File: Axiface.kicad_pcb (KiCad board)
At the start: 2 copper layers, 55.4 x 36.3 mm, 30 parts, among them J1 Conn_01x02, J10 Conn_01x03, J11 Conn_01x04, J2 Conn_01x03, J3 Conn_01x03, J4 Conn_01x03, J5 Conn_01x03, J6 Conn_01x03, J7 Conn_01x03, J8 Conn_01x03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

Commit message: Mise à jour du schéma et pcb
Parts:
- added H1: MountingHole_Pad, MountingHole:MountingHole_2.7mm_M2.5_Pad, F.Cu at (91.7, 132.3)
- added H2: MountingHole_Pad, MountingHole:MountingHole_2.7mm_M2.5_Pad, F.Cu at (91.7, 100.8)
- added H3: MountingHole_Pad, MountingHole:MountingHole_2.7mm_M2.5_Pad, F.Cu at (146.1, 100.8)
- added H4: MountingHole_Pad, MountingHole:MountingHole_2.7mm_M2.5_Pad, F.Cu at (146.1, 132.3)
- C1, C4, C5, C6, C7: moved to F.Cu
- U3, U4, U5: footprint Converter_DCDC:Converter_DCDC_TRACO_TSR-1_THT -> Convert_DCDC:Converter_DCDC_TRACO_TSR-2_THT
- moved C4 20.6 mm to (113.2, 123.2)
- moved C5 15.8 mm to (145.0, 107.7), turned to 270 degrees
- moved C7 15.3 mm to (144.8, 126.5)
- moved C6 15.3 mm to (144.8, 115.4)
- moved C1 3.98 mm to (110.0, 111.0), turned to 0 degrees
- moved J8 1.65 mm to (126.1, 106.9)
- moved J5 1.57 mm to (140.3, 106.9)
- moved J2 1.53 mm to (133.2, 106.9)
- moved D1 1.27 mm to (98.4, 103.4)
- moved J3 1.09 mm to (126.1, 119.3)
- moved R2 1.02 mm to (104.3, 103.4)
- moved R3 1.02 mm to (104.3, 116.1)
- moved R4 1.02 mm to (104.3, 128.8)
- moved J9 0.97 mm to (140.3, 119.3)
- moved J6 0.90 mm to (133.2, 119.3)
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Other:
- board size 55.4 x 36.3 mm -> 60.8 x 37.8 mm

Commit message: Mise à jour avant routage
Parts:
- R2, R3, R4: value R -> 1.8k
- moved D3 2.03 mm to (98.9, 130.9)
- moved R4 2.03 mm to (104.3, 130.8)
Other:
- board text added: "-"
- board text added: "Direction"
- board text added: "RX_CPU"
- board text added: "TX_CPU"
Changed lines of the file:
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@@
   (general
     (thickness 1.6)
-    (drawings 13)
+    (drawings 17)
     (tracks 0)
     (zones 0)
@@
     (35 F.Paste user)
     (36 B.SilkS user)
-    (37 F.SilkS user)
+    (37 F.SilkS user hide)
     (38 B.Mask user)
     (39 F.Mask user)
@@
     (tags capacitor)
     (attr smd)
-    (fp_text reference C2 (at -3.432 0) (layer B.SilkS)
+    (fp_text reference C2 (at -0.13 -2.032) (layer B.SilkS)
       (effects (font (size 1 1) (thickness 0.15)) (justify mirror))
     )
@@
     (tags capacitor)
     (attr smd)
-    (fp_text reference C3 (at 3.302 0) (layer B.SilkS)
+    (fp_text reference C3 (at 3.556 0) (layer B.SilkS)
       (effects (font (size 1 1) (thickness 0.15)) (justify mirror))
     )
@@
   )
   (module LED_SMD:LED_1206_3216Metric (layer F.Cu)
-    (at 98.936 128.828)
+    (at 98.936 130.86)
     (descr "LED SMD 1206 (3216 Metric), square (rectangular) end terminal, IPC_7351 nominal, (Body size source: http://www.tortai-tech.com/upload/download/2011102023233369053.pdf), generated with kicad-footprint-generator")
     (tags diode)
     (attr smd)
-    (fp_text reference D3 (at 0 -1.82) (layer F.SilkS)
+    (fp_text reference D3 (at -0.13 1.982) (layer F.SilkS)
       (effects (font (size 1 1) (thickness 0.15)))
     )
@@
       (effects (font (size 1 1) (thickness 0.15)))
     )
-    (fp_text user - (at -4 0 90) (layer F.SilkS)
+    (fp_text user - (at 0 3.81 90) (layer F.SilkS)
       (effects (font (size 1.5 1.5) (thickness 0.15)))
     )
-    (fp_text user + (at 9 0 90) (layer F.SilkS)
+    (fp_text user + (at 5.08 3.81 90) (layer F.SilkS)
       (effects (font (size 1.5 1.5) (thickness 0.15)))
     )
@@
     (tags resistor)
     (attr smd)
-    (fp_text reference R1 (at -3.172 0) (layer B.SilkS)
+    (fp_text reference R1 (at 3.686 0) (layer B.SilkS)
       (effects (font (size 1 1) (thickness 0.15)) (justify mirror))
     )
@@
       (effects (font (size 1 1) (thickness 0.15)))
     )
-    (fp_text value R (at 0 1.82) (layer F.Fab)
+    (fp_text value 1.8k (at 0 1.82) (layer F.Fab)
       (effects (font (size 1 1) (thickness 0.15)))
     )
@@
       (effects (font (size 1 1) (thickness 0.15)))
     )
-    (fp_text value R (at 0 1.82) (layer F.Fab)
+    (fp_text value 1.8k (at 0 1.82) (layer F.Fab)
       (effects (font (size 1 1) (thickness 0.15)))
     )
@@
   )
   (module Resistor_SMD:R_1206_3216Metric (layer F.Cu)
-    (at 104.27 128.778)
+    (at 104.27 130.81)
     (descr "Resistor SMD 1206 (3216 Metric), square (rectangular) end terminal, IPC_7351 nominal, (Body size source: http://www.tortai-tech.com/upload/download/2011102023233369053.pdf), generated with kicad-footprint-generator")
     (tags resistor)
     (attr smd)
-    (fp_text reference R4 (at 0 -1.82) (layer F.SilkS)
-      (effects (font (size 1 1) (thickness 0.15)))
-    )
-    (fp_text value R (at 0 1.82) (layer F.Fab)
+    (fp_text reference R4 (at 0 2.032) (layer F.SilkS)
+      (effects (font (size 1 1) (thickness 0.15)))
+    )
+    (fp_text value 1.8k (at 0 1.82) (layer F.Fab)
       (effects (font (size 1 1) (thickness 0.15)))
     )
@@
     (tags "CMS SOT")
     (attr smd)
-    (fp_text reference U1 (at 3.404 4.166) (layer B.SilkS)
+    (fp_text reference U1 (at 3.404 4.674) (layer B.SilkS)
       (effects (font (size 1 1) (thickness 0.15)) (justify mirror))
     )
@@
       (effects (font (size 1 1) (thickness 0.15)) (justify mirror))
     )
-    (fp_text user %R (at 0 0 270) (layer B.Fab)
+    (fp_text user %R (at 0 0) (layer B.Fab)
       (effects (font (size 0.8 0.8) (thickness 0.12)) (justify mirror))
     )
@@
       (net 2 GND))
   )
+  (gr_text RX_CPU (at 99.568 127.254) (layer F.SilkS)
+    (effects (font (size 1 1) (thickness 0.1)))
+  )
+  (gr_text TX_CPU (at 99.568 124.714) (layer F.SilkS)
+    (effects (font (size 1 1) (thickness 0.1)))
+  )
+  (gr_text Direction (at 99.822 121.92) (layer F.SilkS)
+    (effects (font (size 1 1) (thickness 0.1)))
+  )
+  (gr_text - (at 97.79 119.634 180) (layer F.SilkS)
+    (effects (font (size 1.5 1.5) (thickness 0.3)))
+  )
   (dimension 31.4579 (width 0.15) (layer Dwgs.User)

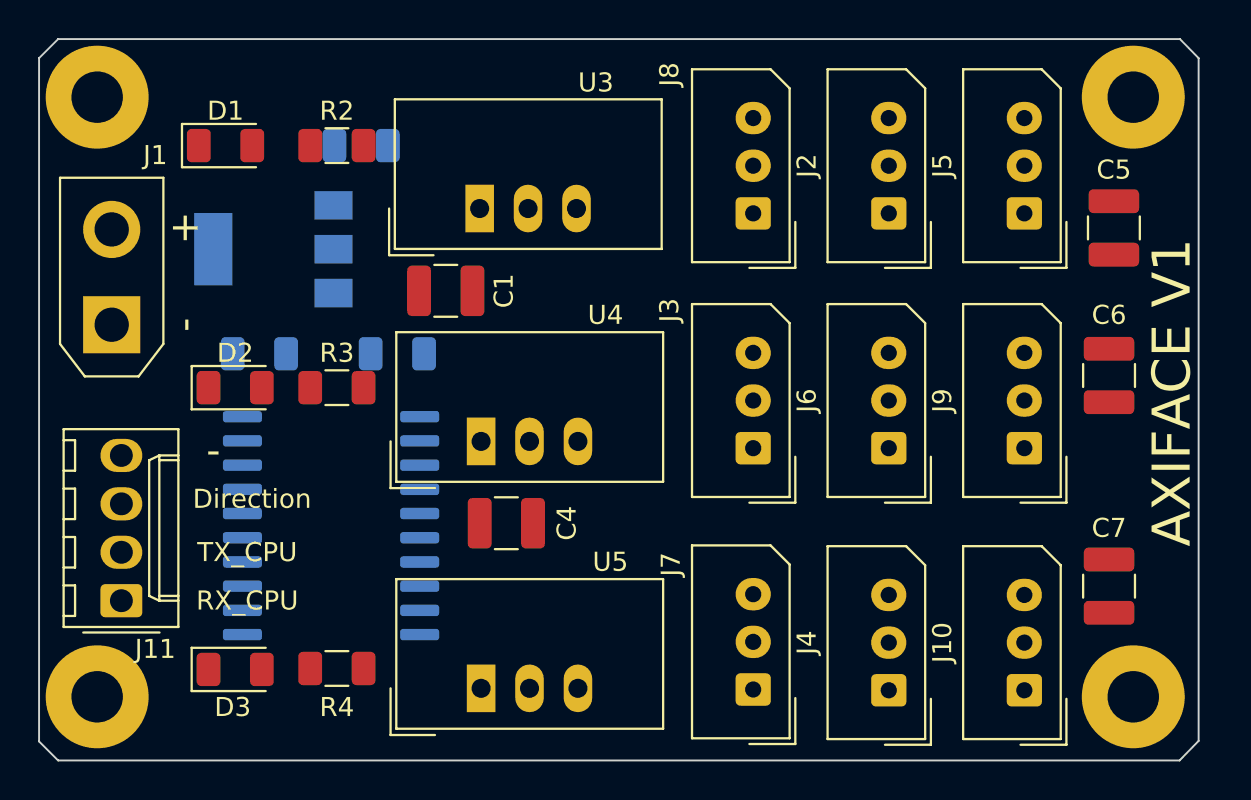
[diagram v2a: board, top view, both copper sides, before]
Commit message: Mise à jour schéma + routage
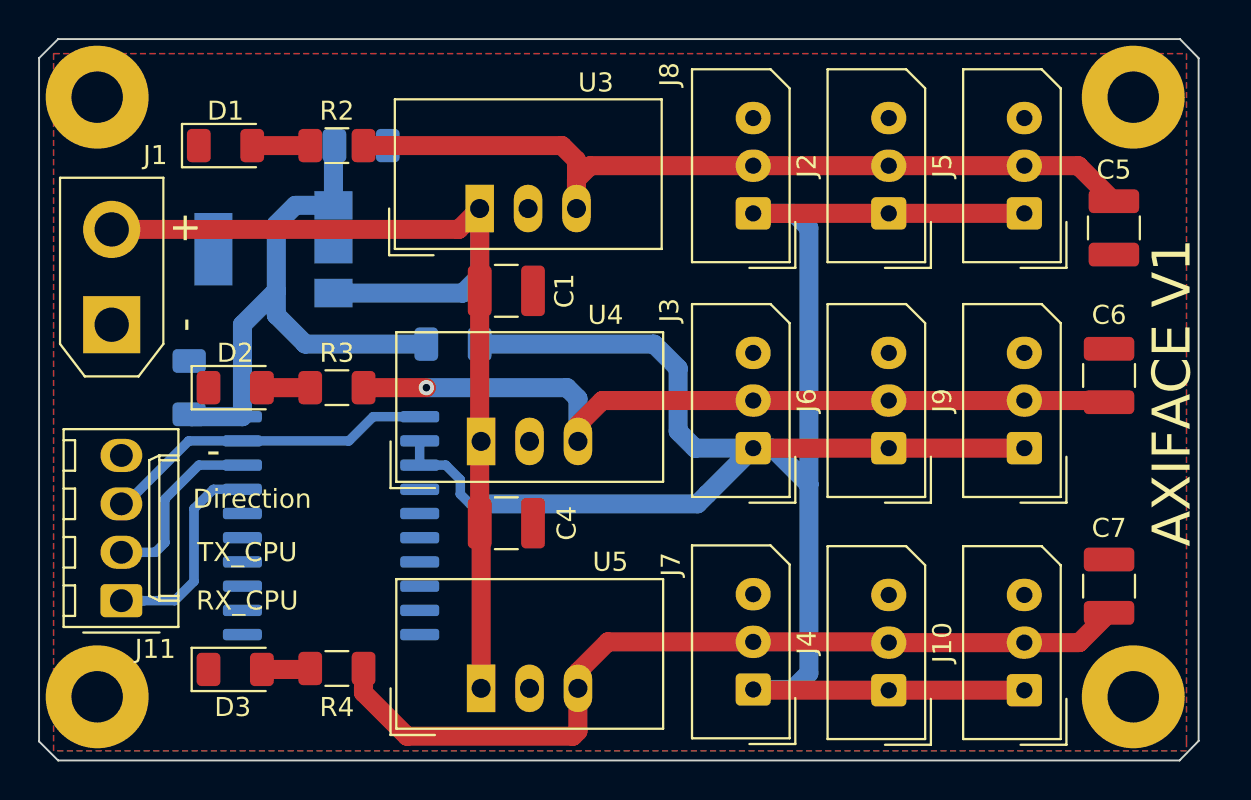
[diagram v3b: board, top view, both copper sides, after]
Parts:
- moved C3 11.1 mm to (96.5, 116.1), turned to 270 degrees
- moved R1 10.2 mm to (110.4, 113.8), turned to 0 degrees
- moved C1 3.18 mm to (113.2, 111.0)
- turned U2 to 180 degrees
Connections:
- J11 pad 1: /RX_CPU -> /TX_CPU
- J11 pad 2: /TX_CPU -> /RX_CPU
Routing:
- net /AxBus: track 0.00 -> 116.1 mm
- net /VBAT: track 0.00 -> 57.1 mm
- net /9V_AX_#3: track 0.00 -> 45.9 mm
- net /9V_AX_#1: track 0.00 -> 44.8 mm
- net /9V_AX_#2: track 0.00 -> 43.0 mm, vias 0 -> 1
- net VCC: track 0.00 -> 30.0 mm
- net /DIRECTION: track 0.00 -> 17.5 mm
- net /TX_CPU: track 0.00 -> 12.2 mm
- net /RX_CPU: track 0.00 -> 10.6 mm
- net Net-(D1-Pad2): track 0.00 -> 3.04 mm
- net Net-(D3-Pad2): track 0.00 -> 2.55 mm
- net Net-(D2-Pad2): track 0.00 -> 2.53 mm
- added copper zone on B.Cu, net GND
- added copper zone on F.Cu, net GND

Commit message: Dernières évolutions mineures avant mise en fabrication
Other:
- board text added: "+"
- board text added: "."
- board text added: "2019"
- board text added: "Data"
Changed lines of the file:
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@@
   (general
     (thickness 1.6)
-    (drawings 17)
+    (drawings 28)
     (tracks 117)
     (zones 0)
@@
   )
   (setup
-    (last_trace_width 1)
+    (last_trace_width 0.3)
     (user_trace_width 0.5)
     (user_trace_width 1)
@@
       (net 2 GND))
   )
+  (gr_text 2019 (at 147.066 124.206 90) (layer B.SilkS)
+    (effects (font (size 1.5 1.5) (thickness 0.15)) (justify mirror))
+  )
+  (gr_text . (at 110.49 115.57) (layer B.SilkS)
+    (effects (font (size 3 3) (thickness 0.5)))
+  )
+  (gr_text Data (at 129.54 106.934) (layer B.SilkS)
+    (effects (font (size 1 1) (thickness 0.1)) (justify mirror))
+  )
+  (gr_text + (at 129.032 104.14 270) (layer B.SilkS)
+    (effects (font (size 1.5 1.5) (thickness 0.3)))
+  )
+  (gr_text - (at 129.032 101.6 270) (layer B.SilkS)
+    (effects (font (size 1.5 1.5) (thickness 0.3)))
+  )
+  (gr_text - (at 129.032 126.746 270) (layer F.SilkS)
+    (effects (font (size 1.5 1.5) (thickness 0.3)))
+  )
+  (gr_text - (at 136.144 126.746 270) (layer F.SilkS)
+    (effects (font (size 1.5 1.5) (thickness 0.3)))
+  )
+  (gr_text - (at 136.144 113.792 270) (layer F.SilkS)
+    (effects (font (size 1.5 1.5) (thickness 0.3)))
+  )
+  (gr_text - (at 136.144 101.6 270) (layer F.SilkS)
+    (effects (font (size 1.5 1.5) (thickness 0.3)))
+  )
+  (gr_text - (at 129.032 113.792 270) (layer F.SilkS)
+    (effects (font (size 1.5 1.5) (thickness 0.3)))
+  )
+  (gr_text - (at 129.032 101.6 270) (layer F.SilkS)
+    (effects (font (size 1.5 1.5) (thickness 0.3)))
+  )
   (gr_text RX_CPU (at 99.568 127.254) (layer F.SilkS)

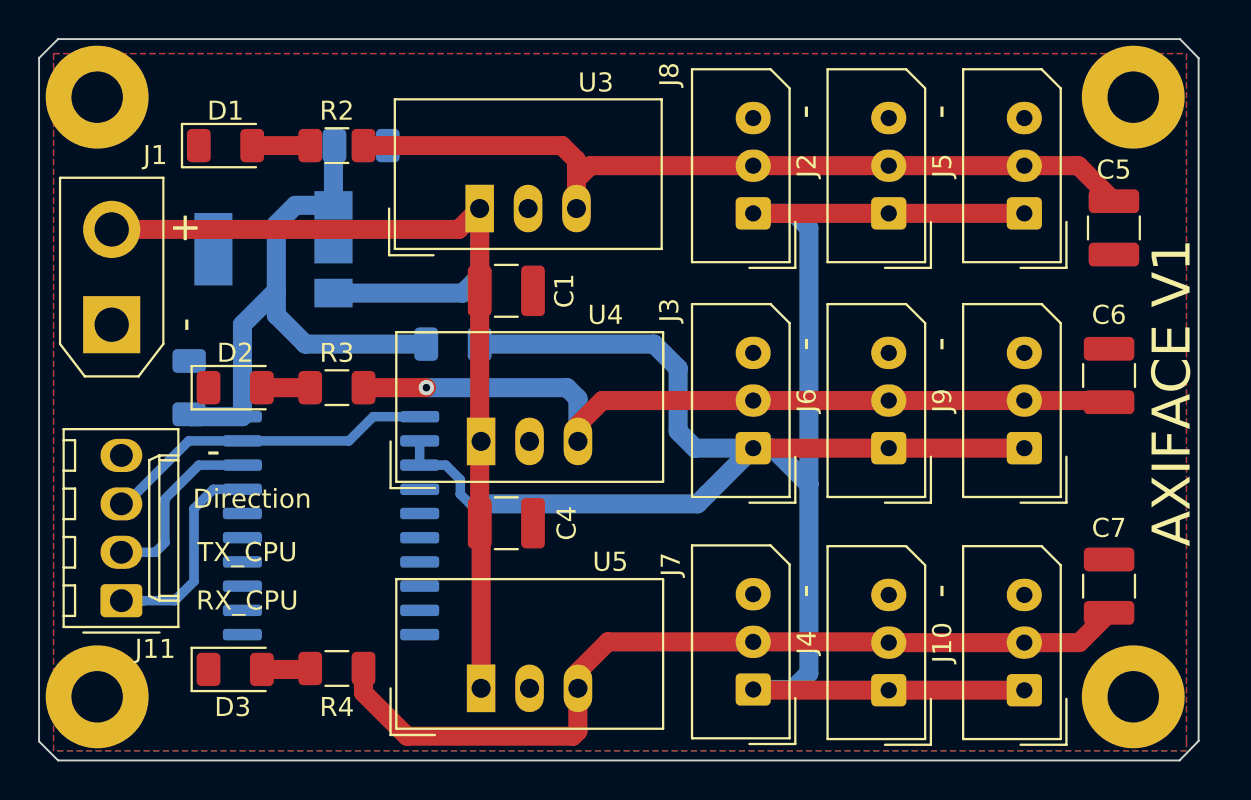
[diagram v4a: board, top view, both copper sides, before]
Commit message: Correction erreur d'empreinte sur les Traco 9V
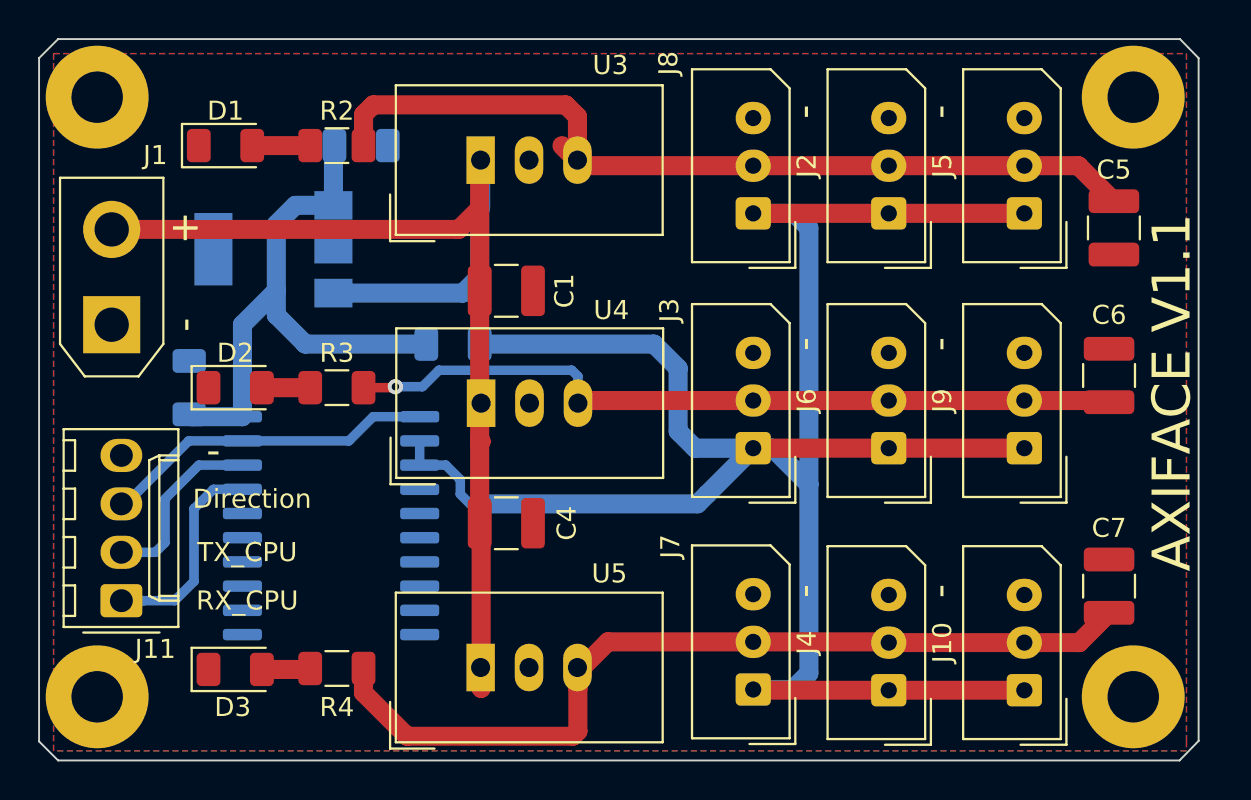
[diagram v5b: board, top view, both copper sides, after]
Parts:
- moved U3 2.54 mm to (111.8, 104.1)
- moved U4 2.01 mm to (111.8, 116.9)
- moved U5 1.09 mm to (111.8, 130.8)
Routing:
- net /VBAT: track 57.1 -> 61.8 mm
- net /9V_AX_#2: track 43.0 -> 41.1 mm
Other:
- board text added: "AXIFACE V1.1"
- board text removed: "AXIFACE V1"

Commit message: #1 Correction sérigraphie RX_CPU<->TX_CPU sur la couche supérieure
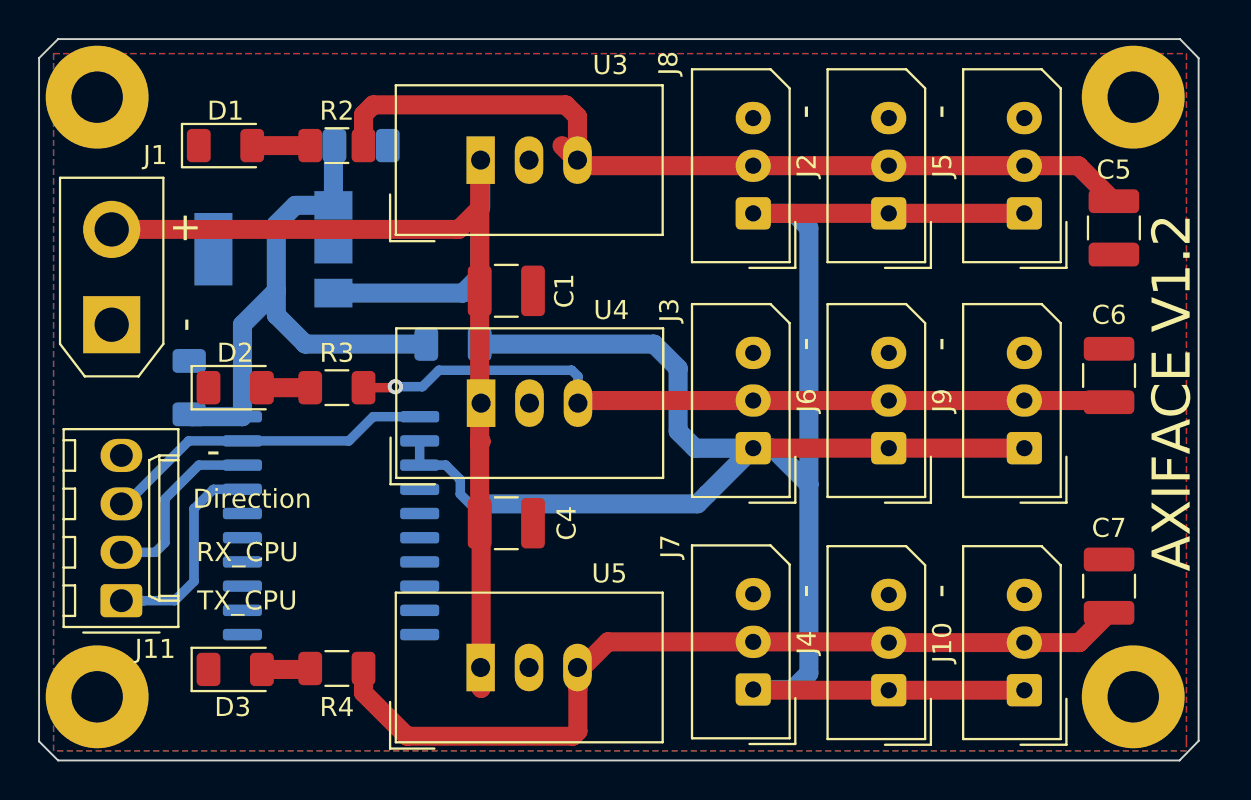
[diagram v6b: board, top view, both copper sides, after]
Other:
- board text added: "AXIFACE V1.2"
- board text removed: "AXIFACE V1.1"
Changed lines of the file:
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@@
   )
   (setup
-    (last_trace_width 0.5)
+    (last_trace_width 0.3)
     (user_trace_width 0.5)
     (user_trace_width 1)
@@
     (effects (font (size 1.5 1.5) (thickness 0.3)))
   )
-  (gr_text RX_CPU (at 99.568 127.254) (layer F.SilkS)
+  (gr_text TX_CPU (at 99.568 127.254) (layer F.SilkS)
     (effects (font (size 1 1) (thickness 0.1)))
   )
-  (gr_text TX_CPU (at 99.568 124.714) (layer F.SilkS)
+  (gr_text RX_CPU (at 99.568 124.714) (layer F.SilkS)
     (effects (font (size 1 1) (thickness 0.1)))
   )
@@
   (gr_line (start 148.479 135.636) (end 89.646 135.636) (layer Edge.Cuts) (width 0.1))
   (gr_line (start 149.479 98.79) (end 149.479 134.6106) (layer Edge.Cuts) (width 0.1))
-  (gr_text "AXIFACE V1.1" (at 148.082 116.332 90) (layer F.SilkS)
+  (gr_text "AXIFACE V1.2" (at 148.082 116.332 90) (layer F.SilkS)
     (effects (font (size 2 2) (thickness 0.15)))
   )
